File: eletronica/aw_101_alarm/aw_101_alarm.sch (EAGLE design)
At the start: 41 parts, among them IC1 ATTINY2313V, IC2 4511N, Q1 4MHz, T2 2N2222, T3 2N2222, T4 2N2222, T5 2N2222, T6 2N2222, X1 UPDOWN, X2 TIMER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

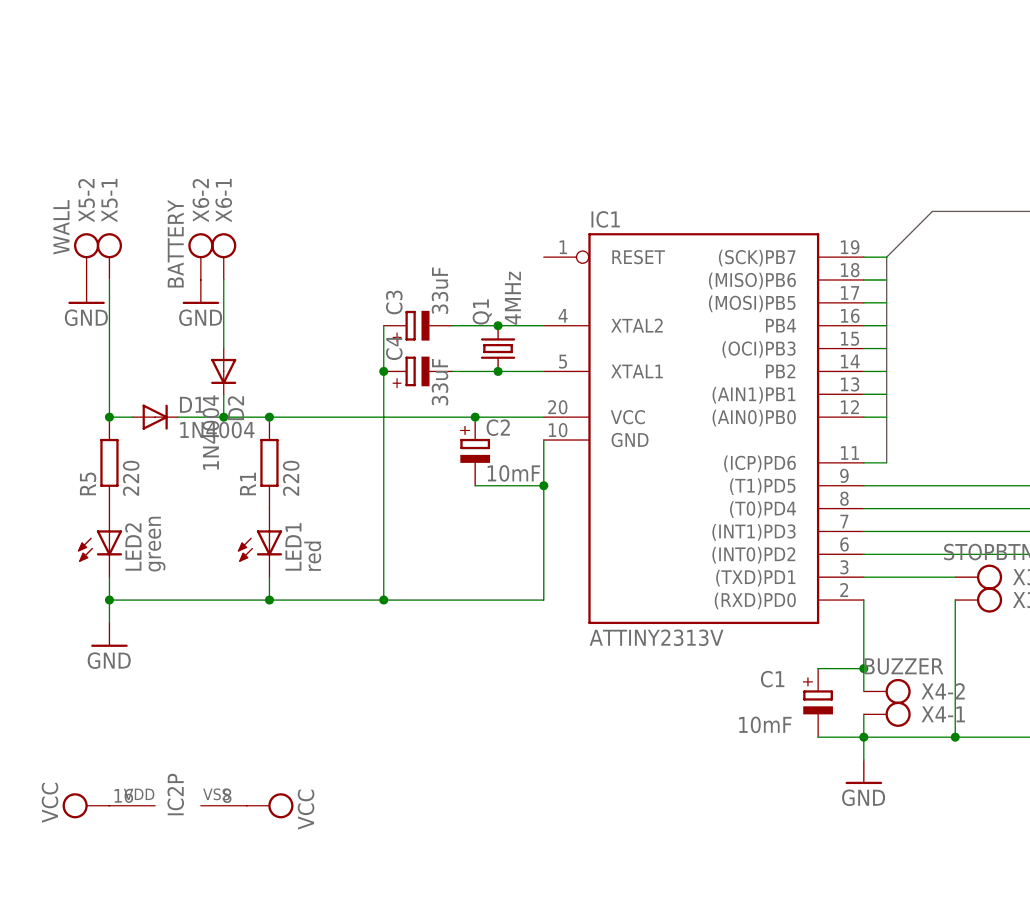
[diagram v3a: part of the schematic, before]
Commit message: 
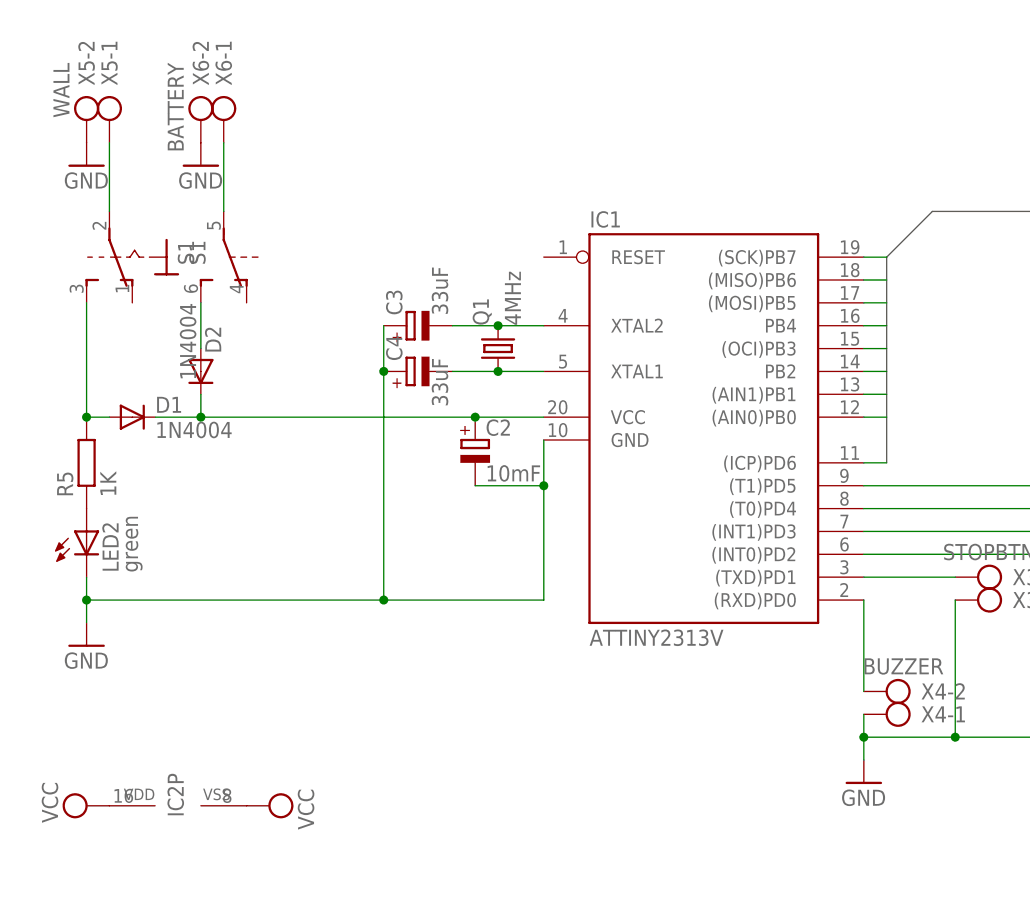
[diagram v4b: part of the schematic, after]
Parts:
- removed C1: 10mF, rcl:CPOL-EUE2.5-6
- removed LED1: red, led:LED5MM
- removed R1: 220, rcl:R-EU_0207/10
- added S1: (no value), switch:320-938
- R5: value 220 -> 1K
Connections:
- new net N$12: D2.A, S1B.S
- net GND: no longer C1.-, LED1.C
- net N$10: no longer C1.+
- net N$2: now also S11.S; no longer X5-1.KL
- net N$3: now also S11.P, X5-1.KL; no longer D2.A, X6-1.KL
- net N$4: now also S1B.P, X6-1.KL; no longer LED1.A, R1.1
- net VCC: no longer R1.2
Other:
- moved on the sheet: D1, D2, LED2, R5, X5-1, X5-2, X6-1, X6-2
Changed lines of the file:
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@@
 </classes>
 <parts>
-<part name="R1" library="rcl" deviceset="R-EU_" device="0207/10" value="220"/>
-<part name="LED1" library="led" deviceset="LED" device="5MM" value="red"/>
 <part name="IC1" library="atmel" deviceset="AT90S2313" device="P" value="ATTINY2313V"/>
 <part name="X1" library="con-ptr500" deviceset="AK500/3" device="" value="UPDOWN"/>
@@
 <part name="X6" library="con-ptr500" deviceset="AK500/2" device="" value="BATTERY"/>
 <part name="GND11" library="supply1" deviceset="GND" device=""/>
-<part name="R5" library="rcl" deviceset="R-EU_" device="0207/10" value="220"/>
+<part name="R5" library="rcl" deviceset="R-EU_" device="0207/10" value="1K"/>
 <part name="LED2" library="led" deviceset="LED" device="5MM" value="green"/>
 <part name="GND1" library="supply1" deviceset="GND" device=""/>
@@
 <part name="GND7" library="supply1" deviceset="GND" device=""/>
 <part name="X4" library="con-ptr500" deviceset="AK500/2" device="" value="BUZZER"/>
-<part name="C1" library="rcl" deviceset="CPOL-EU" device="E2.5-6" value="10mF"/>
 <part name="Q1" library="crystal" deviceset="CRYSTAL" device="HC49U70" value="4MHz"/>
 <part name="C3" library="rcl" deviceset="CPOL-EU" device="E2.5-6" value="33uF"/>
 <part name="C4" library="rcl" deviceset="CPOL-EU" device="E2.5-6" value="33uF"/>
+<part name="S1" library="switch" deviceset="320-938" device=""/>
 </parts>
 <sheets>
@@
 </plain>
 <instances>
-<instance part="R1" gate="G$1" x="20.32" y="55.88" rot="R90"/>
-<instance part="LED1" gate="G$1" x="20.32" y="48.26"/>
 <instance part="IC1" gate="G$1" x="68.58" y="58.42"/>
 <instance part="X1" gate="-1" x="137.16" y="48.26" rot="R180"/>
@@
 <instance part="SUPPLY3" gate="G$1" x="0" y="17.78" rot="R90"/>
 <instance part="SUPPLY4" gate="G$1" x="20.32" y="17.78" rot="R270"/>
-<instance part="X5" gate="-1" x="2.54" y="81.28" rot="R270"/>
-<instance part="X5" gate="-2" x="0" y="81.28" rot="R270"/>
-<instance part="GND10" gate="1" x="0" y="73.66"/>
-<instance part="X6" gate="-1" x="15.24" y="81.28" rot="R270"/>
-<instance part="X6" gate="-2" x="12.7" y="81.28" rot="R270"/>
-<instance part="GND11" gate="1" x="12.7" y="73.66"/>
-<instance part="R5" gate="G$1" x="2.54" y="55.88" rot="R90"/>
-<instance part="LED2" gate="G$1" x="2.54" y="48.26"/>
-<instance part="GND1" gate="1" x="2.54" y="35.56"/>
-<instance part="D1" gate="1" x="7.62" y="60.96"/>
-<instance part="D2" gate="1" x="15.24" y="66.04" rot="R270"/>
+<instance part="X5" gate="-1" x="2.54" y="96.52" rot="R270"/>
+<instance part="X5" gate="-2" x="0" y="96.52" rot="R270"/>
+<instance part="GND10" gate="1" x="0" y="88.9"/>
+<instance part="X6" gate="-1" x="15.24" y="96.52" rot="R270"/>
+<instance part="X6" gate="-2" x="12.7" y="96.52" rot="R270"/>
+<instance part="GND11" gate="1" x="12.7" y="88.9"/>
+<instance part="R5" gate="G$1" x="0" y="55.88" rot="R90"/>
+<instance part="LED2" gate="G$1" x="0" y="48.26"/>
+<instance part="GND1" gate="1" x="0" y="35.56"/>
+<instance part="D1" gate="1" x="5.08" y="60.96"/>
+<instance part="D2" gate="1" x="12.7" y="66.04" smashed="yes" rot="R270">
+<attribute name="NAME" x="13.1826" y="71.12" size="1.778" layer="95" rot="R270"/>
+<attribute name="VALUE" x="10.3886" y="73.66" size="1.778" layer="96" rot="R270"/>
+</instance>
 <instance part="GND7" gate="1" x="86.36" y="20.32"/>
 <instance part="X4" gate="-1" x="91.44" y="27.94" rot="R180"/>
 <instance part="X4" gate="-2" x="91.44" y="30.48" rot="R180"/>
-<instance part="C1" gate="G$1" x="81.28" y="30.48" smashed="yes">
-<attribute name="NAME" x="74.803" y="30.9626" size="1.778" layer="95"/>
-<attribute name="VALUE" x="72.263" y="25.8826" size="1.778" layer="96"/>
-</instance>
 <instance part="Q1" gate="G$1" x="45.72" y="68.58" rot="R90"/>
 <instance part="C3" gate="G$1" x="35.56" y="71.12" rot="R90"/>
@@
 <attribute name="VALUE" x="40.1574" y="62.103" size="1.778" layer="96" rot="R90"/>
 </instance>
+<instance part="S1" gate="B" x="15.24" y="78.74" rot="R180"/>
+<instance part="S1" gate="1" x="5.08" y="78.74" rot="R180"/>
 </instances>
 <busses>
@@
 <pinref part="LED2" gate="G$1" pin="C"/>
 <pinref part="GND1" gate="1" pin="GND"/>
-<wire x1="2.54" y1="38.1" x2="2.54" y2="40.64" width="0.1524" layer="91"/>
-<pinref part="LED1" gate="G$1" pin="C"/>
-<wire x1="2.54" y1="40.64" x2="2.54" y2="43.18" width="0.1524" layer="91"/>
-<wire x1="20.32" y1="43.18" x2="20.32" y2="40.64" width="0.1524" layer="91"/>
+<wire x1="0" y1="38.1" x2="0" y2="40.64" width="0.1524" layer="91"/>
+<wire x1="0" y1="40.64" x2="0" y2="43.18" width="0.1524" layer="91"/>
 <pinref part="IC1" gate="G$1" pin="GND"/>
 <wire x1="50.8" y1="58.42" x2="50.8" y2="53.34" width="0.1524" layer="91"/>
@@
 <pinref part="C3" gate="G$1" pin="+"/>
 <pinref part="C4" gate="G$1" pin="+"/>
-<wire x1="33.02" y1="40.64" x2="20.32" y2="40.64" width="0.1524" layer="91"/>
 <wire x1="33.02" y1="71.12" x2="33.02" y2="66.04" width="0.1524" layer="91"/>
 <wire x1="33.02" y1="66.04" x2="33.02" y2="40.64" width="0.1524" layer="91"/>
 <junction x="33.02" y="66.04"/>
 <junction x="33.02" y="40.64"/>
-<wire x1="20.32" y1="40.64" x2="2.54" y2="40.64" width="0.1524" layer="91"/>
-<junction x="20.32" y="40.64"/>
-<junction x="2.54" y="40.64"/>
+<wire x1="33.02" y1="40.64" x2="0" y2="40.64" width="0.1524" layer="91"/>
+<junction x="0" y="40.64"/>
 </segment>
 <segment>
@@
 <pinref part="GND7" gate="1" pin="GND"/>
 <wire x1="86.36" y1="22.86" x2="86.36" y2="25.4" width="0.1524" layer="91"/>
-<pinref part="C1" gate="G$1" pin="-"/>
 <wire x1="86.36" y1="25.4" x2="86.36" y2="27.94" width="0.1524" layer="91"/>
-<wire x1="81.28" y1="25.4" x2="86.36" y2="25.4" width="0.1524" layer="91"/>
 <junction x="86.36" y="25.4"/>
 <pinref part="X3" gate="-1" pin="KL"/>
@@
 </segment>
 <segment>
-<pinref part="R1" gate="G$1" pin="2"/>
-<wire x1="15.24" y1="60.96" x2="20.32" y2="60.96" width="0.1524" layer="91"/>
-<wire x1="15.24" y1="63.5" x2="15.24" y2="60.96" width="0.1524" layer="91"/>
+<wire x1="12.7" y1="63.5" x2="12.7" y2="60.96" width="0.1524" layer="91"/>
 <pinref part="C2" gate="G$1" pin="+"/>
-<wire x1="20.32" y1="60.96" x2="43.18" y2="60.96" width="0.1524" layer="91"/>
-<junction x="20.32" y="60.96"/>
+<wire x1="12.7" y1="60.96" x2="43.18" y2="60.96" width="0.1524" layer="91"/>
 <pinref part="IC1" gate="G$1" pin="VCC"/>
 <wire x1="43.18" y1="60.96" x2="50.8" y2="60.96" width="0.1524" layer="91"/>
@@
 <pinref part="D2" gate="1" pin="C"/>
 <pinref part="D1" gate="1" pin="C"/>
-<wire x1="10.16" y1="60.96" x2="15.24" y2="60.96" width="0.1524" layer="91"/>
-<junction x="15.24" y="60.96"/>
-</segment>
-</net>
-<net name="N$4" class="0">
-<segment>
-<pinref part="R1" gate="G$1" pin="1"/>
-<pinref part="LED1" gate="G$1" pin="A"/>
+<wire x1="7.62" y1="60.96" x2="12.7" y2="60.96" width="0.1524" layer="91"/>
+<junction x="12.7" y="60.96"/>
 </segment>
 </net>
@@
 <pinref part="IC1" gate="G$1" pin="(TXD)PD1"/>
 <wire x1="96.52" y1="43.18" x2="86.36" y2="43.18" width="0.1524" layer="91"/>
-</segment>
-</net>
-<net name="N$3" class="0">
-<segment>
-<pinref part="X6" gate="-1" pin="KL"/>
-<wire x1="15.24" y1="76.2" x2="15.24" y2="68.58" width="0.1524" layer="91"/>
-<pinref part="D2" gate="1" pin="A"/>
 </segment>
 </net>
@@
 <net name="N$2" class="0">
 <segment>
-<pinref part="X5" gate="-1" pin="KL"/>
 <pinref part="R5" gate="G$1" pin="2"/>
-<wire x1="2.54" y1="76.2" x2="2.54" y2="60.96" width="0.1524" layer="91"/>
 <pinref part="D1" gate="1" pin="A"/>
-<wire x1="2.54" y1="60.96" x2="5.08" y2="60.96" width="0.1524" layer="91"/>
-<junction x="2.54" y="60.96"/>
+<wire x1="0" y1="60.96" x2="2.54" y2="60.96" width="0.1524" layer="91"/>
+<pinref part="S1" gate="1" pin="S"/>
+<wire x1="0" y1="73.66" x2="0" y2="60.96" width="0.1524" layer="91"/>
+<junction x="0" y="60.96"/>
 </segment>
 </net>
@@
 <segment>
 <pinref part="IC1" gate="G$1" pin="(RXD)PD0"/>
-<wire x1="86.36" y1="40.64" x2="86.36" y2="33.02" width="0.1524" layer="91"/>
+<wire x1="86.36" y1="40.64" x2="86.36" y2="30.48" width="0.1524" layer="91"/>
 <pinref part="X4" gate="-2" pin="KL"/>
-<pinref part="C1" gate="G$1" pin="+"/>
-<wire x1="86.36" y1="33.02" x2="86.36" y2="30.48" width="0.1524" layer="91"/>
-<wire x1="81.28" y1="33.02" x2="86.36" y2="33.02" width="0.1524" layer="91"/>
-<junction x="86.36" y="33.02"/>
 </segment>
 </net>
@@
 </segment>
 </net>
+<net name="N$3" class="0">
+<segment>
+<pinref part="X5" gate="-1" pin="KL"/>
+<pinref part="S1" gate="1" pin="P"/>
+<wire x1="2.54" y1="91.44" x2="2.54" y2="83.82" width="0.1524" layer="91"/>
+</segment>
+</net>
+<net name="N$4" class="0">
+<segment>
+<pinref part="X6" gate="-1" pin="KL"/>
+<pinref part="S1" gate="B" pin="P"/>
+<wire x1="15.24" y1="91.44" x2="15.24" y2="83.82" width="0.1524" layer="91"/>
+</segment>
+</net>
+<net name="N$12" class="0">
+<segment>
+<pinref part="S1" gate="B" pin="S"/>
+<pinref part="D2" gate="1" pin="A"/>
+<wire x1="12.7" y1="73.66" x2="12.7" y2="68.58" width="0.1524" layer="91"/>
+</segment>
+</net>
